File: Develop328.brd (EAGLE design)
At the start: 100 x 80 mm, 12 parts

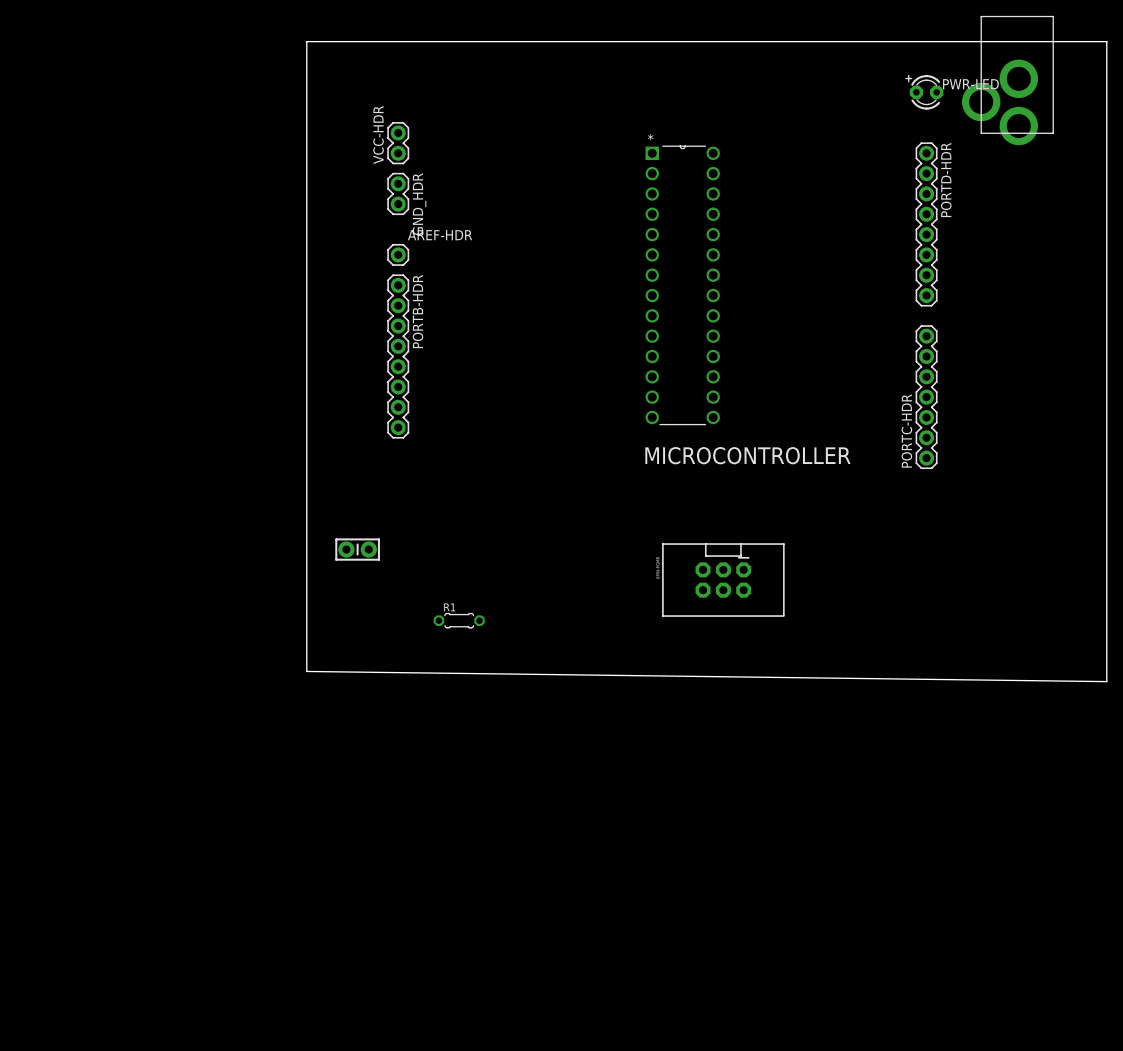
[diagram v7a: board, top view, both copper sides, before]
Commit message: Updated board design and laid out all parts
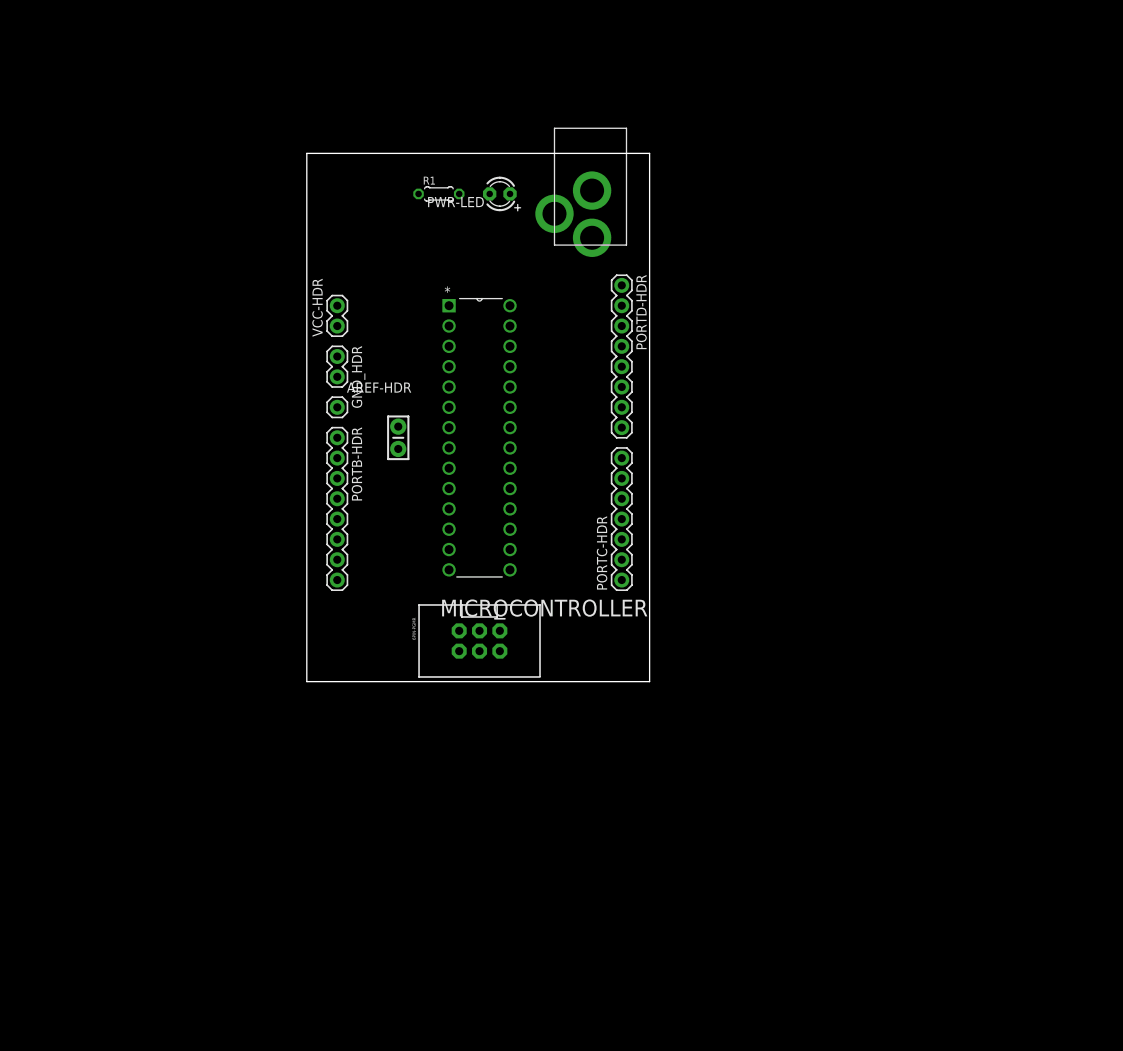
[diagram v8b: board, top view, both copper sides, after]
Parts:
- moved 5V-DC-JACK 55.1 mm to (35.6, 64.8)
- moved PWR-LED 54.8 mm to (24.1, 61.0), turned to 180 degrees
- moved R1 53.4 mm to (16.5, 61.0)
- moved PORTD-HDR 41.5 mm to (39.4, 49.5)
- moved PORTC-HDR 41.0 mm to (39.4, 12.7)
- moved MICROCONTROLLER 31.8 mm to (25.4, 14.0)
- moved 6PIN-PGMR 31.4 mm to (21.6, 5.08)
- moved VCC-HDR 22.9 mm to (3.81, 44.5)
- moved GND_HDR 22.9 mm to (3.81, 40.6)
- moved AREF-HDR 20.5 mm to (3.81, 34.3)
- moved PORTB-HDR 20.5 mm to (3.81, 30.5)
- moved VCC_CAP 14.9 mm to (11.4, 30.5), turned to 270 degrees
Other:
- board size 100 x 80 mm -> 42.9 x 66 mm
